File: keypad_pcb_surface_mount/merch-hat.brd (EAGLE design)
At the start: 65 x 56 mm, 15 parts

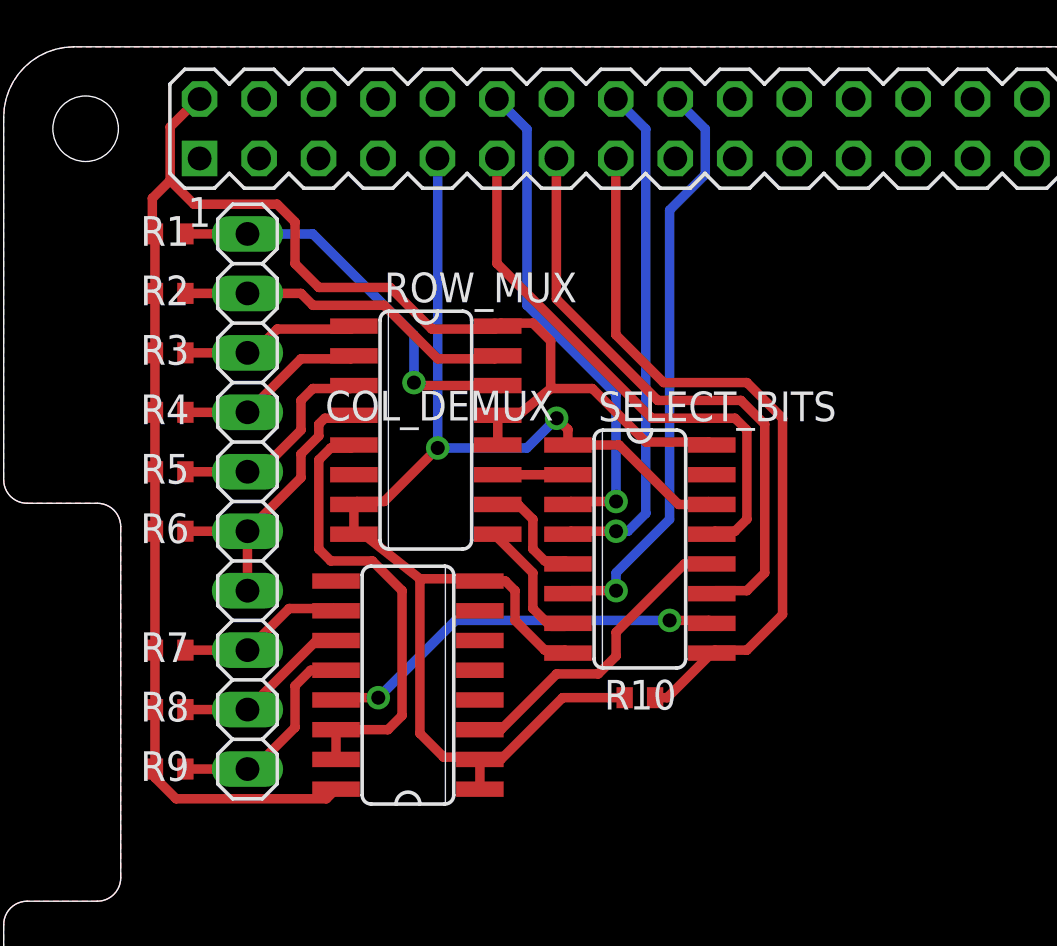
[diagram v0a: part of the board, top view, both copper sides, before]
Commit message: update pcbs to remove clear bug on 74174 chip
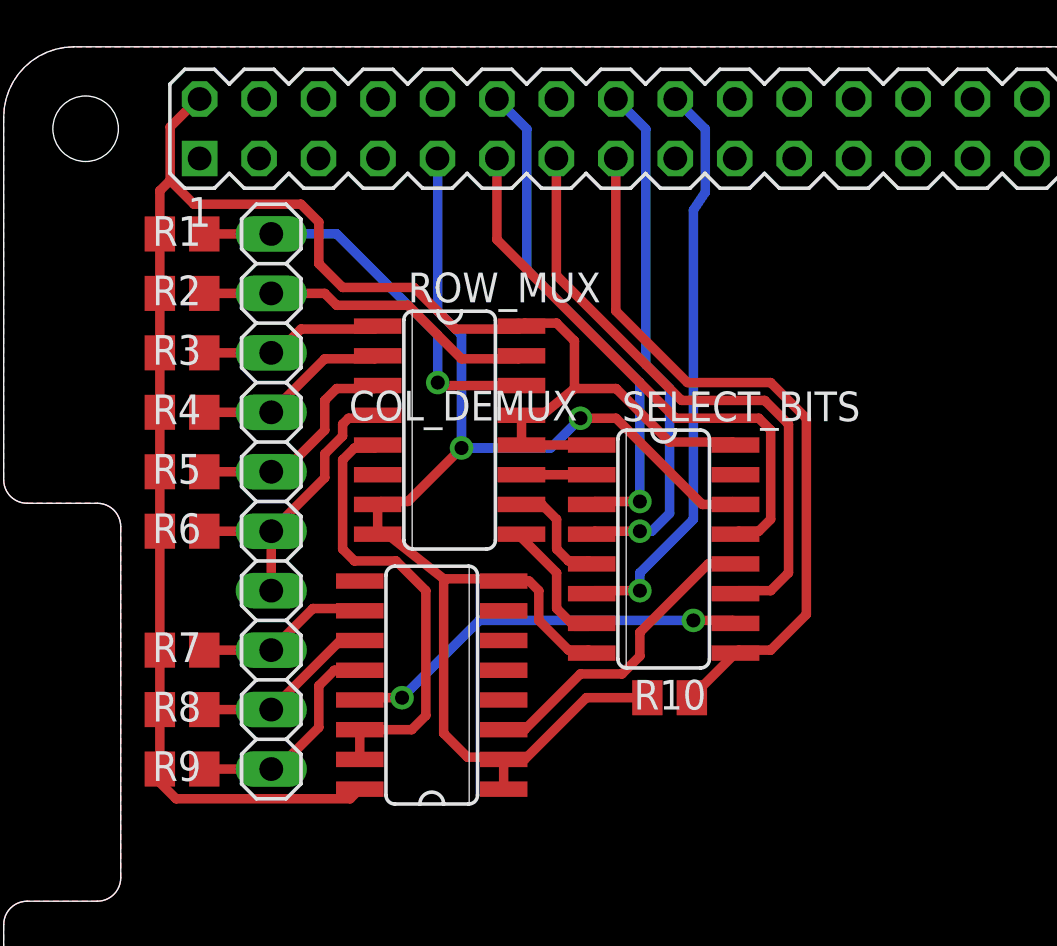
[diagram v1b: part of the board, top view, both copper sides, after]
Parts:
- R1, R10, R2, R3, R4, R5, R6, R7, R8, R9: device resistor:R0402 -> resistor:R0805
- moved R10 1.27 mm to (28.4, 28.2)
- moved COL_DEMUX 1.02 mm to (18.3, 28.7)
- moved ROW_MUX 1.02 mm to (19.1, 39.6)
- moved JP1 1.02 mm to (11.4, 36.6)
- moved SELECT_BITS 1.02 mm to (28.2, 34.5)
- moved R1 0.51 mm to (7.62, 48.0)
- moved R2 0.51 mm to (7.62, 45.5)
- moved R3 0.51 mm to (7.62, 42.9)
- moved R4 0.51 mm to (7.62, 40.4)
- moved R5 0.51 mm to (7.62, 37.8)
- moved R6 0.51 mm to (7.62, 35.3)
- moved R7 0.51 mm to (7.62, 30.2)
- moved R8 0.51 mm to (7.62, 27.7)
- moved R9 0.51 mm to (7.62, 25.1)
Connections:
- net +5V: now also SELECT_BITS.1
- net GND: no longer SELECT_BITS.1
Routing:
- net +5V: track 72.6 -> 77.3 mm
